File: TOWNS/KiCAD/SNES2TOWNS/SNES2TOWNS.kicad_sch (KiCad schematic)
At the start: 12 parts, among them J1 DE9_Receptacle, J6 SNES_CONTROLLER, J7 Slide Switch, J8 ArduinoNANOP1_P15, J9 ArduinoNANOP16_P30, U1 74LS157, U2 74LS157

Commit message: PCB
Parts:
- J6: footprint Connector_PinHeader_2.54mm:PinHeader_1x07_P2.54mm_Vertical -> SNES:SNES_Controller
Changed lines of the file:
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@@
       (effects (font (size 1.27 1.27)))
     )
-    (property "Footprint" "Connector_PinHeader_2.54mm:PinHeader_1x07_P2.54mm_Vertical" (at 44.45 96.52 0)
+    (property "Footprint" "SNES:SNES_Controller" (at 44.45 96.52 0)
       (effects (font (size 1.27 1.27)) hide)
     )

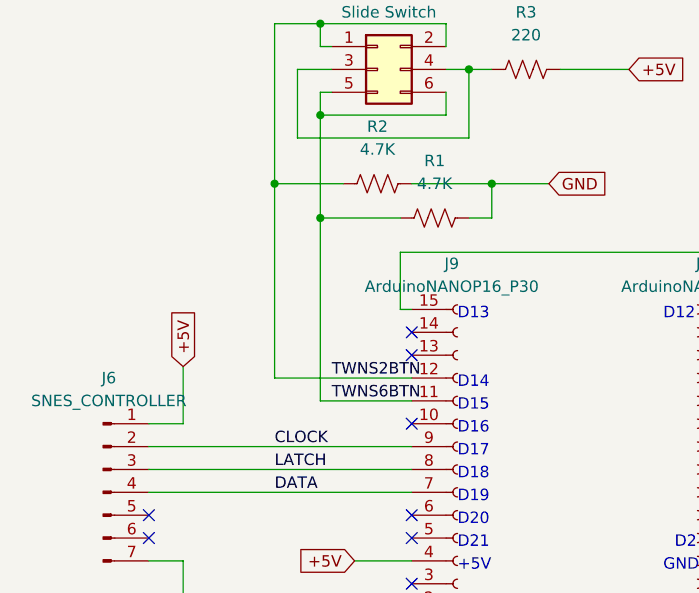
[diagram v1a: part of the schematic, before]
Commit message: Added status LED.
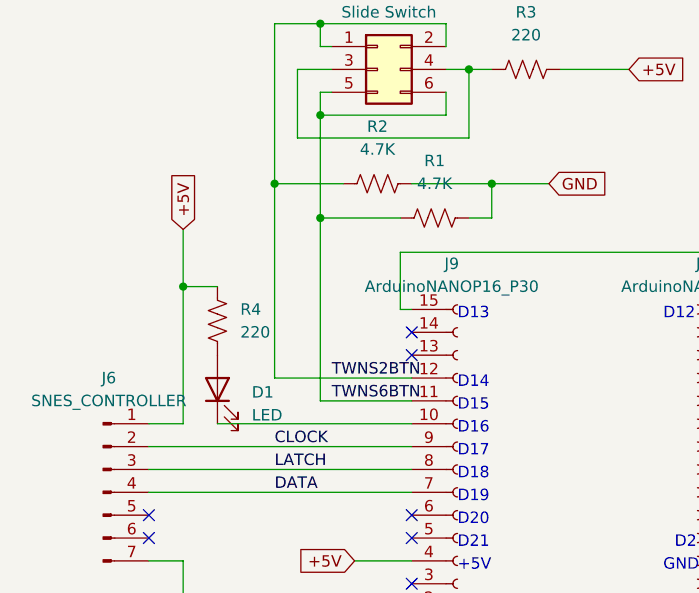
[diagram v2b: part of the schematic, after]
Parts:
- added D1: LED, LED_SMD:LED_0805_2012Metric_Pad1.15x1.40mm_HandSolder, symbol Device:LED
- added R4: 220, Resistor_SMD:R_0805_2012Metric_Pad1.20x1.40mm_HandSolder, symbol Device:R_US
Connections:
- net +5V: now also R4.1
- net at J9.10 (Pin_10): now also D1.1 (K)
- new net: D1.2 (A), R4.2
- no-connect marks 15 -> 14
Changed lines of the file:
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@@
   (junction (at 162.56 124.46) (diameter 0) (color 0 0 0 0)
+  )
+  (junction (at 53.34 73.66) (diameter 0) (color 0 0 0 0)
   )
   (junction (at 87.63 62.23) (diameter 0) (color 0 0 0 0)
@@
   (no_connect (at 201.93 129.54))
   (no_connect (at 115.57 104.14))
-  (no_connect (at 78.74 88.9))
   (no_connect (at 78.74 106.68))
   (no_connect (at 78.74 81.28))
@@
     (stroke (width 0) (type default))
   )
+  (wire (pts (xy 53.34 73.66) (xy 53.34 88.9))
+    (stroke (width 0) (type default))
+  )
   (wire (pts (xy 153.67 137.16) (xy 176.53 137.16))
     (stroke (width 0) (type default))
@@
     (stroke (width 0) (type default))
   )
-  (wire (pts (xy 53.34 82.55) (xy 53.34 88.9))
+  (wire (pts (xy 53.34 67.31) (xy 53.34 73.66))
     (stroke (width 0) (type default))
   )
@@
     (stroke (width 0) (type default))
   )
+  (wire (pts (xy 53.34 73.66) (xy 57.15 73.66))
+    (stroke (width 0) (type default))
+  )
   (wire (pts (xy 245.11 134.62) (xy 245.11 138.43))
     (stroke (width 0) (type default))
@@
     (stroke (width 0) (type default))
   )
+  (wire (pts (xy 57.15 88.9) (xy 78.74 88.9))
+    (stroke (width 0) (type default))
+  )
   (wire (pts (xy 237.49 66.04) (xy 241.3 66.04))
     (stroke (width 0) (type default))
@@
     (effects (font (size 1.27 1.27)) (justify left bottom))
   )
-  (global_label "+5V" (shape input) (at 53.34 82.55 90) (fields_autoplaced)
+  (global_label "+5V" (shape input) (at 53.34 67.31 90) (fields_autoplaced)
     (effects (font (size 1.27 1.27)) (justify left))
-    (property "Intersheetrefs" "${INTERSHEET_REFS}" (at 53.34 75.6943 90)
+    (property "Intersheetrefs" "${INTERSHEET_REFS}" (at 53.34 60.4543 90)
       (effects (font (size 1.27 1.27)) (justify left) hide)
     )
@@
     )
   )
+  (symbol (lib_id "Device:LED") (at 57.15 85.09 90) (unit 1)
+    (in_bom yes) (on_board yes) (dnp no) (fields_autoplaced)
+    (property "Reference" "D1" (at 60.96 85.4075 90)
+      (effects (font (size 1.27 1.27)) (justify right))
+    )
+    (property "Value" "LED" (at 60.96 87.9475 90)
+      (effects (font (size 1.27 1.27)) (justify right))
+    )
+    (property "Footprint" "LED_SMD:LED_0805_2012Metric_Pad1.15x1.40mm_HandSolder" (at 57.15 85.09 0)
+      (effects (font (size 1.27 1.27)) hide)
+    )
+    (property "Datasheet" "~" (at 57.15 85.09 0)
+      (effects (font (size 1.27 1.27)) hide)
+    )
+    (pin "1")
+    (pin "2")
+    (instances
+      (project "SNES2TOWNS"
+        (path "/d12ccb08-8752-4d3d-ad3b-4f570691df19"
+          (reference "D1") (unit 1)
+        )
+      )
+    )
+  )
   (symbol (lib_id "Connector:Conn_01x15_Socket") (at 83.82 93.98 0) (mirror x) (unit 1)
     (in_bom yes) (on_board yes) (dnp no)
@@
         )
       )
+    )
+  )
+  (symbol (lib_id "Device:R_US") (at 57.15 77.47 0) (unit 1)
+    (in_bom yes) (on_board yes) (dnp no) (fields_autoplaced)
+    (property "Reference" "R4" (at 59.69 76.2 0)
+      (effects (font (size 1.27 1.27)) (justify left))
+    )
+    (property "Value" "220" (at 59.69 78.74 0)
+      (effects (font (size 1.27 1.27)) (justify left))
+    )
+    (property "Footprint" "Resistor_SMD:R_0805_2012Metric_Pad1.20x1.40mm_HandSolder" (at 58.166 77.724 90)
+      (effects (font (size 1.27 1.27)) hide)
+    )
+    (property "Datasheet" "~" (at 57.15 77.47 0)
+      (effects (font (size 1.27 1.27)) hide)
+    )
+    (pin "1")
+    (pin "2")
+    (instances
+      (project "SNES2TOWNS"
+        (path "/d12ccb08-8752-4d3d-ad3b-4f570691df19"
+          (reference "R4") (unit 1)
+        )
+      )

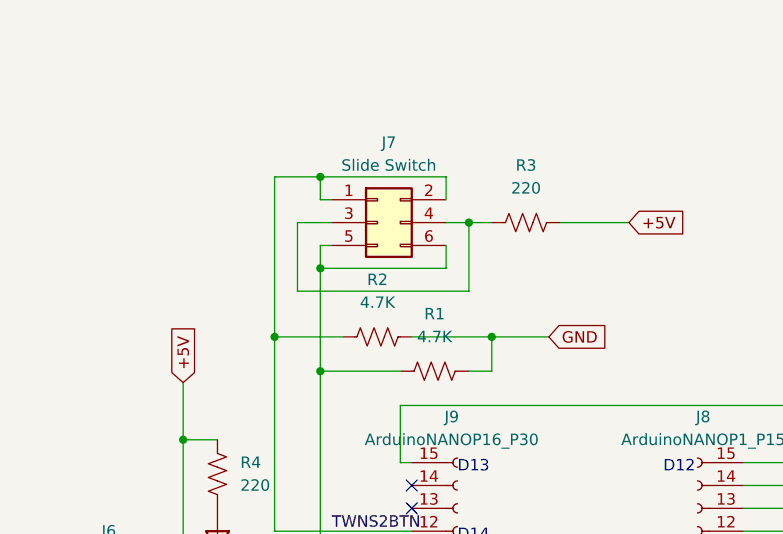
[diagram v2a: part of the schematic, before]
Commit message: Use PCM3TSMTR instead of general SPDT On-Off-On.
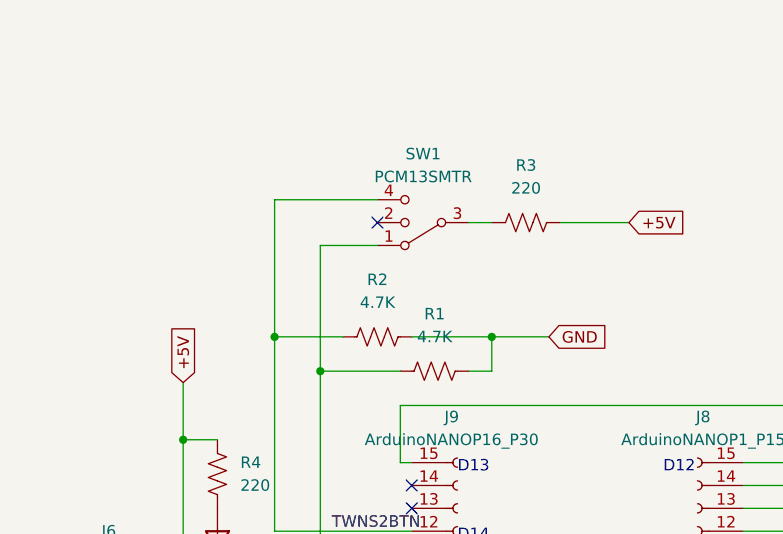
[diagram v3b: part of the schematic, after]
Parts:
- removed J7: Slide Switch, Connector_PinHeader_2.54mm:PinHeader_2x03_P2.54mm_Vertical, symbol Connector_Generic:Conn_02x03_Odd_Even
- added SW1: PCM13SMTR, Button_Switch_SMD:SW_SP3T_PCM13, symbol Switch:SW_SP3T
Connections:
- net TWNS2BTN: now also SW1.4
- net TWNS6BTN: now also SW1.1
- net at R3.1: now also SW1.3
- no-connect marks 14 -> 15
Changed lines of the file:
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@@
   (junction (at 68.58 66.04) (diameter 0) (color 0 0 0 0)
   )
-  (junction (at 68.58 54.61) (diameter 0) (color 0 0 0 0)
-  )
   (junction (at 153.67 91.44) (diameter 0) (color 0 0 0 0)
   )
-  (junction (at 68.58 44.45) (diameter 0) (color 0 0 0 0)
-  )
   (junction (at 162.56 129.54) (diameter 0) (color 0 0 0 0)
   )
@@
   )
   (junction (at 245.11 123.19) (diameter 0) (color 0 0 0 0)
-  )
-  (junction (at 85.09 49.53) (diameter 0) (color 0 0 0 0)
   )
   (junction (at 162.56 87.63) (diameter 0) (color 0 0 0 0)
@@
   (no_connect (at 78.74 101.6))
   (no_connect (at 78.74 78.74))
+  (no_connect (at 74.93 49.53))
   (no_connect (at 115.57 109.22))
   (no_connect (at 78.74 99.06))
@@
   (no_connect (at 49.53 99.06))
   (no_connect (at 49.53 101.6))
-  (wire (pts (xy 69.85 49.53) (xy 66.04 49.53))
-    (stroke (width 0) (type default))
-  )
   (wire (pts (xy 78.74 76.2) (xy 77.47 76.2))
     (stroke (width 0) (type default))
@@
     (stroke (width 0) (type default))
   )
+  (wire (pts (xy 63.5 46.99) (xy 63.5 62.23))
+    (stroke (width 0) (type default))
+  )
   (wire (pts (xy 254 123.19) (xy 245.11 123.19))
     (stroke (width 0) (type default))
@@
     (stroke (width 0) (type default))
   )
-  (wire (pts (xy 66.04 57.15) (xy 85.09 57.15))
-    (stroke (width 0) (type default))
-  )
   (wire (pts (xy 115.57 91.44) (xy 146.05 91.44))
     (stroke (width 0) (type default))
@@
     (stroke (width 0) (type default))
   )
-  (wire (pts (xy 68.58 44.45) (xy 82.55 44.45))
+  (wire (pts (xy 63.5 46.99) (xy 74.93 46.99))
     (stroke (width 0) (type default))
   )
@@
     (stroke (width 0) (type default))
   )
-  (wire (pts (xy 85.09 57.15) (xy 85.09 49.53))
-    (stroke (width 0) (type default))
-  )
   (wire (pts (xy 262.89 53.34) (xy 262.89 106.68))
     (stroke (width 0) (type default))
@@
     (stroke (width 0) (type default))
   )
-  (wire (pts (xy 69.85 46.99) (xy 68.58 46.99))
-    (stroke (width 0) (type default))
-  )
   (wire (pts (xy 125.73 46.99) (xy 125.73 69.85))
     (stroke (width 0) (type default))
@@
     (stroke (width 0) (type default))
   )
-  (wire (pts (xy 68.58 44.45) (xy 63.5 44.45))
-    (stroke (width 0) (type default))
-  )
   (wire (pts (xy 162.56 139.7) (xy 176.53 139.7))
     (stroke (width 0) (type default))
@@
     (stroke (width 0) (type default))
   )
-  (wire (pts (xy 82.55 49.53) (xy 85.09 49.53))
+  (wire (pts (xy 74.93 52.07) (xy 68.58 52.07))
     (stroke (width 0) (type default))
   )
@@
     (stroke (width 0) (type default))
   )
-  (wire (pts (xy 82.55 54.61) (xy 82.55 52.07))
-    (stroke (width 0) (type default))
-  )
   (wire (pts (xy 130.81 54.61) (xy 176.53 54.61))
     (stroke (width 0) (type default))
@@
     (stroke (width 0) (type default))
   )
-  (wire (pts (xy 68.58 54.61) (xy 68.58 66.04))
-    (stroke (width 0) (type default))
-  )
-  (wire (pts (xy 82.55 44.45) (xy 82.55 46.99))
+  (wire (pts (xy 68.58 52.07) (xy 68.58 66.04))
     (stroke (width 0) (type default))
   )
@@
     (stroke (width 0) (type default))
   )
-  (wire (pts (xy 68.58 52.07) (xy 68.58 54.61))
-    (stroke (width 0) (type default))
-  )
   (wire (pts (xy 162.56 139.7) (xy 162.56 147.32))
     (stroke (width 0) (type default))
@@
     (stroke (width 0) (type default))
   )
-  (wire (pts (xy 69.85 52.07) (xy 68.58 52.07))
-    (stroke (width 0) (type default))
-  )
   (wire (pts (xy 128.27 49.53) (xy 176.53 49.53))
     (stroke (width 0) (type default))
@@
     (stroke (width 0) (type default))
   )
-  (wire (pts (xy 66.04 49.53) (xy 66.04 57.15))
-    (stroke (width 0) (type default))
-  )
   (wire (pts (xy 138.43 116.84) (xy 176.53 116.84))
     (stroke (width 0) (type default))
@@
     (stroke (width 0) (type default))
   )
-  (wire (pts (xy 68.58 46.99) (xy 68.58 44.45))
-    (stroke (width 0) (type default))
-  )
   (wire (pts (xy 115.57 86.36) (xy 140.97 86.36))
     (stroke (width 0) (type default))
@@
     (stroke (width 0) (type default))
   )
-  (wire (pts (xy 68.58 54.61) (xy 82.55 54.61))
-    (stroke (width 0) (type default))
-  )
   (wire (pts (xy 162.56 124.46) (xy 176.53 124.46))
     (stroke (width 0) (type default))
@@
   )
   (wire (pts (xy 162.56 87.63) (xy 189.23 87.63))
-    (stroke (width 0) (type default))
-  )
-  (wire (pts (xy 63.5 44.45) (xy 63.5 62.23))
     (stroke (width 0) (type default))
   )
@@
     )
   )
+  (symbol (lib_id "Switch:SW_SP3T") (at 80.01 49.53 180) (unit 1)
+    (in_bom yes) (on_board yes) (dnp no) (fields_autoplaced)
+    (property "Reference" "SW1" (at 80.01 41.91 0)
+      (effects (font (size 1.27 1.27)))
+    )
+    (property "Value" "PCM13SMTR" (at 80.01 44.45 0)
+      (effects (font (size 1.27 1.27)))
+    )
+    (property "Footprint" "Button_Switch_SMD:SW_SP3T_PCM13" (at 95.885 53.975 0)
+      (effects (font (size 1.27 1.27)) hide)
+    )
+    (property "Datasheet" "~" (at 95.885 53.975 0)
+      (effects (font (size 1.27 1.27)) hide)
+    )
+    (pin "1")
+    (pin "2")
+    (pin "3")
+    (pin "4")
+    (instances
+      (project "SNES2TOWNS"
+        (path "/d12ccb08-8752-4d3d-ad3b-4f570691df19"
+          (reference "SW1") (unit 1)
+        )
+      )
+    )
+  )
   (symbol (lib_id "Device:R_US") (at 81.28 66.04 90) (unit 1)
     (in_bom yes) (on_board yes) (dnp no) (fields_autoplaced)
@@
         )
       )
-    )
-  )
-  (symbol (lib_id "Connector_Generic:Conn_02x03_Odd_Even") (at 74.93 49.53 0) (unit 1)
-    (in_bom yes) (on_board yes) (dnp no) (fields_autoplaced)
-    (property "Reference" "J7" (at 76.2 40.64 0)
-      (effects (font (size 1.27 1.27)))
-    )
-    (property "Value" "Slide Switch" (at 76.2 43.18 0)
-      (effects (font (size 1.27 1.27)))
-    )
-    (property "Footprint" "Connector_PinHeader_2.54mm:PinHeader_2x03_P2.54mm_Vertical" (at 74.93 49.53 0)
-      (effects (font (size 1.27 1.27)) hide)
-    )
-    (property "Datasheet" "~" (at 74.93 49.53 0)
-      (effects (font (size 1.27 1.27)) hide)
-    )
-    (pin "1")
-    (pin "2")
-    (pin "3")
-    (pin "4")
-    (pin "5")
-    (pin "6")
-    (instances
-      (project "SNES2TOWNS"
-        (path "/d12ccb08-8752-4d3d-ad3b-4f570691df19"
-          (reference "J7") (unit 1)
-        )
-      )

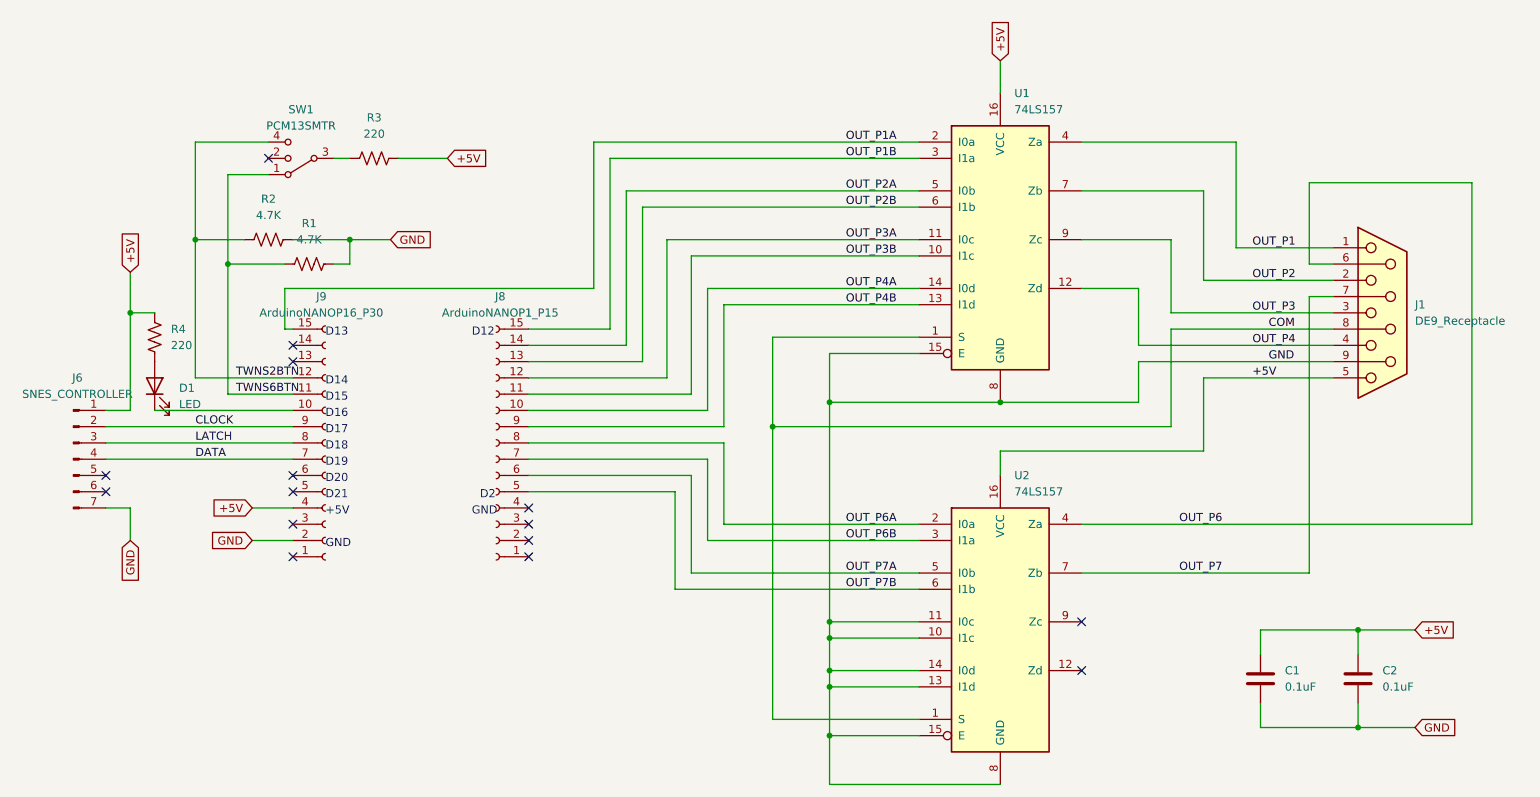
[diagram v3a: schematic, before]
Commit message: Avoid pin 13 not to keep on-board LED on.  Pull-up (instead of ground) unused input pins of LS157.
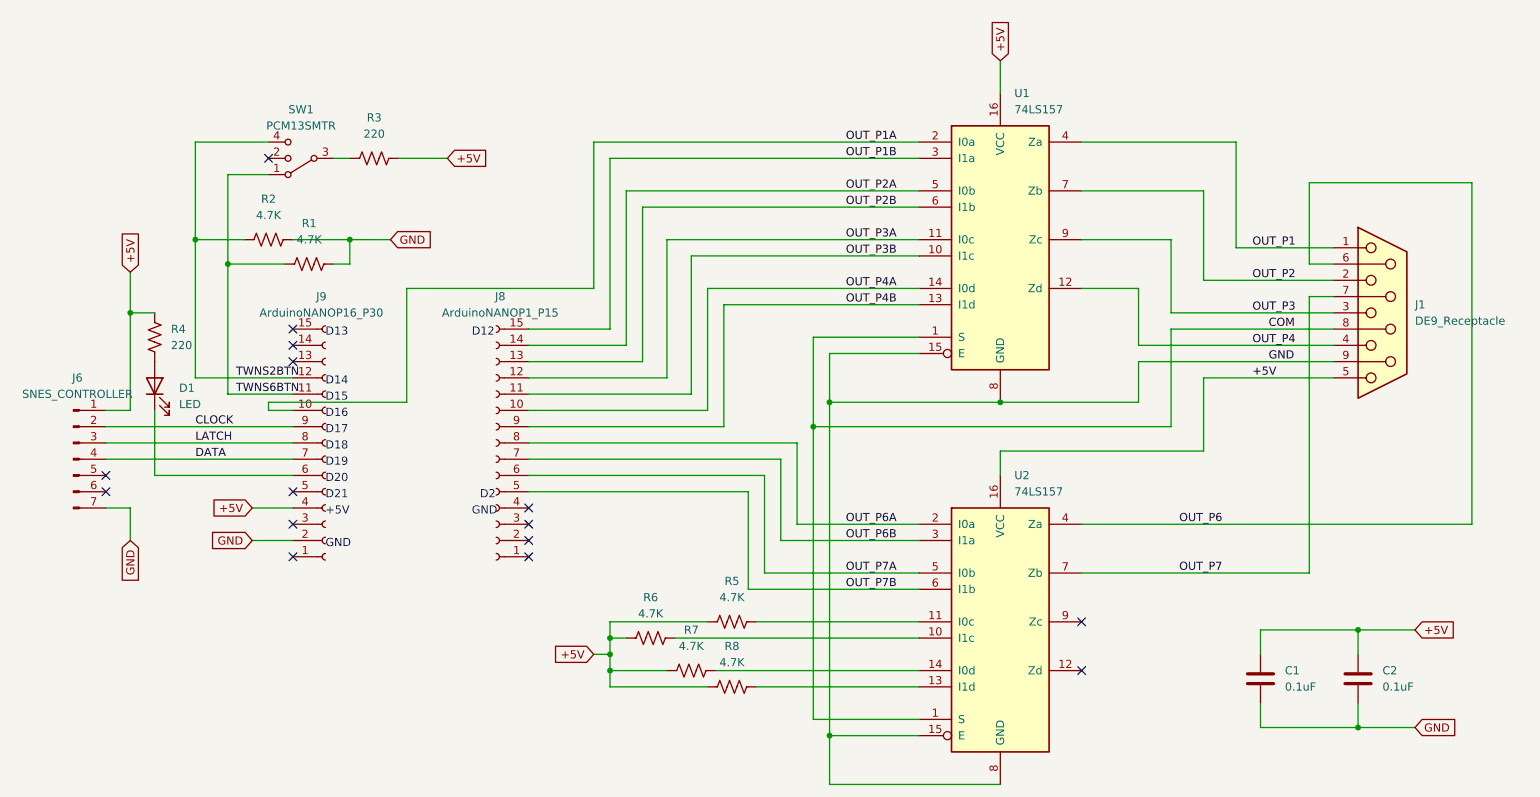
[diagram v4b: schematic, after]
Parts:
- added R5, R6, R7, R8: 4.7K, Resistor_SMD:R_0805_2012Metric_Pad1.20x1.40mm_HandSolder, symbol Device:R_US
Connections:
- net +5V: now also R5.1, R6.1, R7.1, R8.1
- net GND: no longer U2.10 (I1c), U2.11 (I0c), U2.13 (I1d), U2.14 (I0d)
- net OUT_P1A: now also J9.10 (Pin_10); no longer J9.15 (Pin_15)
- net at D1.1 (K): now also J9.6 (Pin_6); no longer J9.10 (Pin_10)
- new net: R6.2, U2.10 (I1c)
- new net: R5.2, U2.11 (I0c)
- new net: R8.2, U2.13 (I1d)
- new net: R7.2, U2.14 (I0d)
